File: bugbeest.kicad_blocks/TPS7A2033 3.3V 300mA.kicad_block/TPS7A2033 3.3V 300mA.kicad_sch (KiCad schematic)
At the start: 4 parts, among them U2 AP2127K-3.3

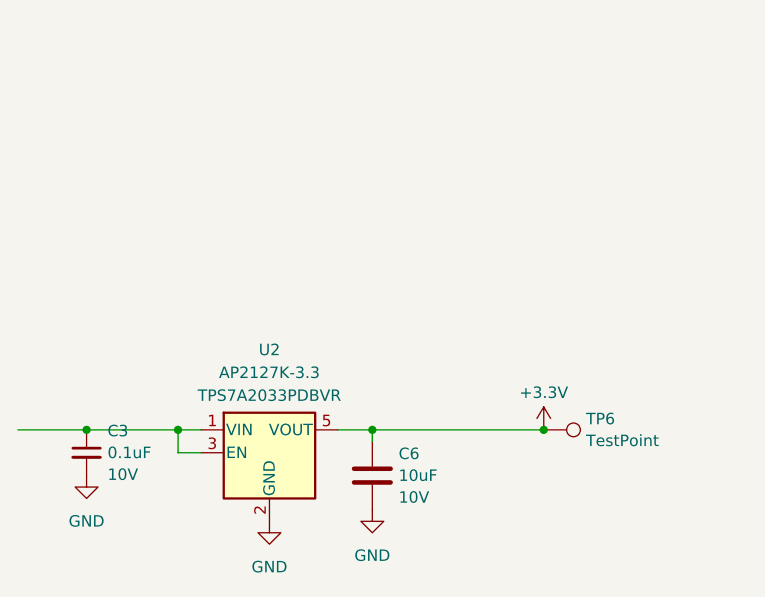
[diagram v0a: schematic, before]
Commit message: debugged design blocks, added encoder footprint
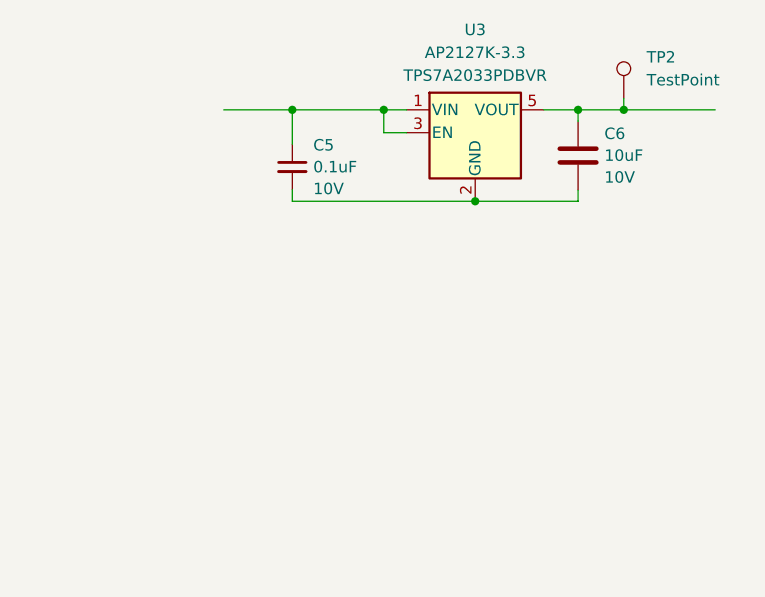
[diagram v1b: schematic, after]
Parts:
- removed C3: 0.1uF, Capacitor_SMD:C_0402_1005Metric, symbol Device:C_Small
- added C5: 0.1uF, Capacitor_SMD:C_0402_1005Metric, symbol Device:C_Small
- TP2: renamed from TP6; now left out of the parts list
- renumbered U2 to U3
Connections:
- net at U3.1 (VIN), U3.3 (EN): now also C5.1
- net +3.3V: no longer names the net of C6.1, TP2.1, U3.5 (VOUT)
- net GND: no longer names the net of C6.2, U3.2 (GND)
- net GND: now also C5.2
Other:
- moved on the sheet: TP2, U3
